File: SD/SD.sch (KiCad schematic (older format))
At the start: 13 parts, among them J1 PMOD1, J2 SD_Card

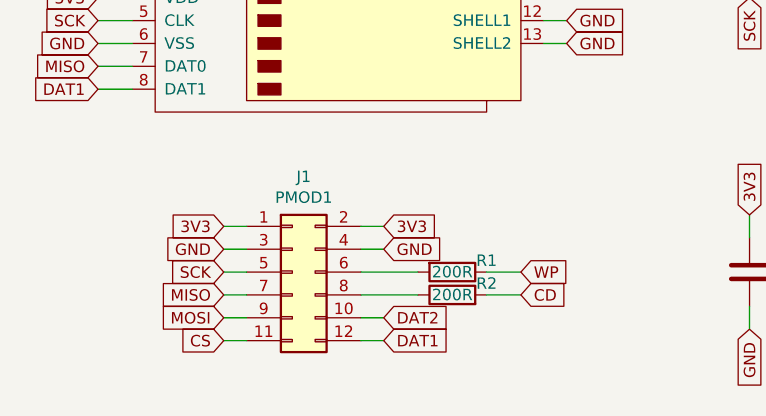
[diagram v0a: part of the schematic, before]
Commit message: Fixing pinouts and pictures
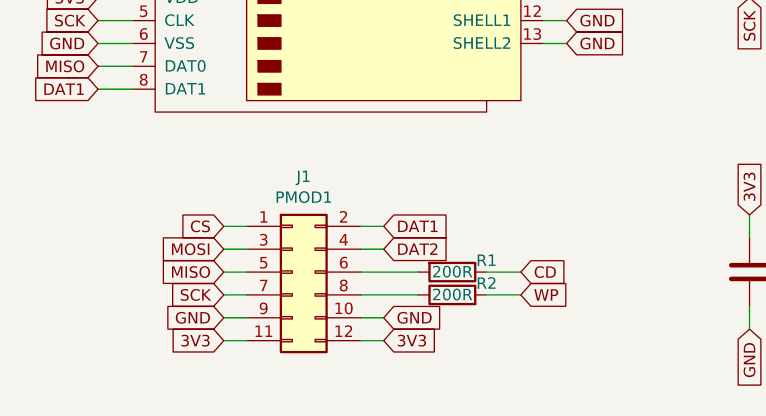
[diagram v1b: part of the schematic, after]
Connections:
- net 3V3: now also J1.11 (Pin_11), J1.12 (Pin_12); no longer J1.1 (Pin_1), J1.2 (Pin_2)
- net CD: now also R1.1; no longer R2.2
- net CS: now also J1.1 (Pin_1); no longer J1.11 (Pin_11)
- net DAT1: now also J1.2 (Pin_2); no longer J1.12 (Pin_12)
- net DAT2: now also J1.4 (Pin_4); no longer J1.10 (Pin_10)
- net GND: now also J1.10 (Pin_10), J1.9 (Pin_9); no longer J1.3 (Pin_3), J1.4 (Pin_4)
- net MISO: now also J1.5 (Pin_5); no longer J1.7 (Pin_7)
- net MOSI: now also J1.3 (Pin_3); no longer J1.9 (Pin_9)
- net SCK: now also J1.7 (Pin_7); no longer J1.5 (Pin_5)
- net WP: now also R2.2; no longer R1.1
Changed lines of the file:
@@
 EESchema Schematic File Version 4
+LIBS:SD-cache
 EELAYER 26 0
 EELAYER END
@@
 	1    0    0    -1
 $EndComp
+Text GLabel 6500 5400 0    50   Input ~ 0
+3V3
+Text GLabel 6500 5300 0    50   Input ~ 0
+GND
+Text GLabel 7200 5400 2    50   Input ~ 0
+3V3
+Text GLabel 7200 5300 2    50   Input ~ 0
+GND
 Text GLabel 6500 4900 0    50   Input ~ 0
-3V3
+CS
 Text GLabel 6500 5000 0    50   Input ~ 0
-GND
+MOSI
+Text GLabel 6500 5100 0    50   Input ~ 0
+MISO
+Text GLabel 6500 5200 0    50   Input ~ 0
+SCK
+Text GLabel 7200 5000 2    50   Input ~ 0
+DAT2
 Text GLabel 7200 4900 2    50   Input ~ 0
-3V3
-Text GLabel 7200 5000 2    50   Input ~ 0
-GND
-Text GLabel 6500 5400 0    50   Input ~ 0
-CS
-Text GLabel 6500 5300 0    50   Input ~ 0
-MOSI
-Text GLabel 6500 5200 0    50   Input ~ 0
-MISO
-Text GLabel 6500 5100 0    50   Input ~ 0
-SCK
-Text GLabel 7200 5300 2    50   Input ~ 0
-DAT2
-Text GLabel 7200 5400 2    50   Input ~ 0
 DAT1
+Text GLabel 7800 5100 2    50   Input ~ 0
+CD
 Text GLabel 7800 5200 2    50   Input ~ 0
-CD
-Text GLabel 7800 5100 2    50   Input ~ 0
 WP
 Wire Wire Line
